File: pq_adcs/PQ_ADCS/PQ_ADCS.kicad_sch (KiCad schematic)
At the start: 55 parts, among them J1 CES-110-02-L-S, J10 Pico-Clasp_01x09, J11 Pico-Clasp_01x15, J12 CES-102-02-L-S, J2 CES-110-02-L-S, J3 CES-110-02-L-S, J4 CES-110-02-L-S, J5 Pico-Clasp_01x03, J6 Pico-Clasp_01x10, J7 Pico-Clasp_01x10, J8 Pico-Clasp_01x10, J9 Pico-Clasp_01x10, U1 LPV542, U2 LPV542, U3 LPV542, U4 IIM-42652, U5 BD2606MVV, U6 TMUX1108RSVR, U7 TCN75AVOA713

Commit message: document formating
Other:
- company: (none) -> NanoSat Lab UPC
- title: (none) -> ADCS subsyetm schematic
- moved on the sheet: C1, C10, C11, C12, C13, C14, C2, C3, C4, C5, C6, C7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

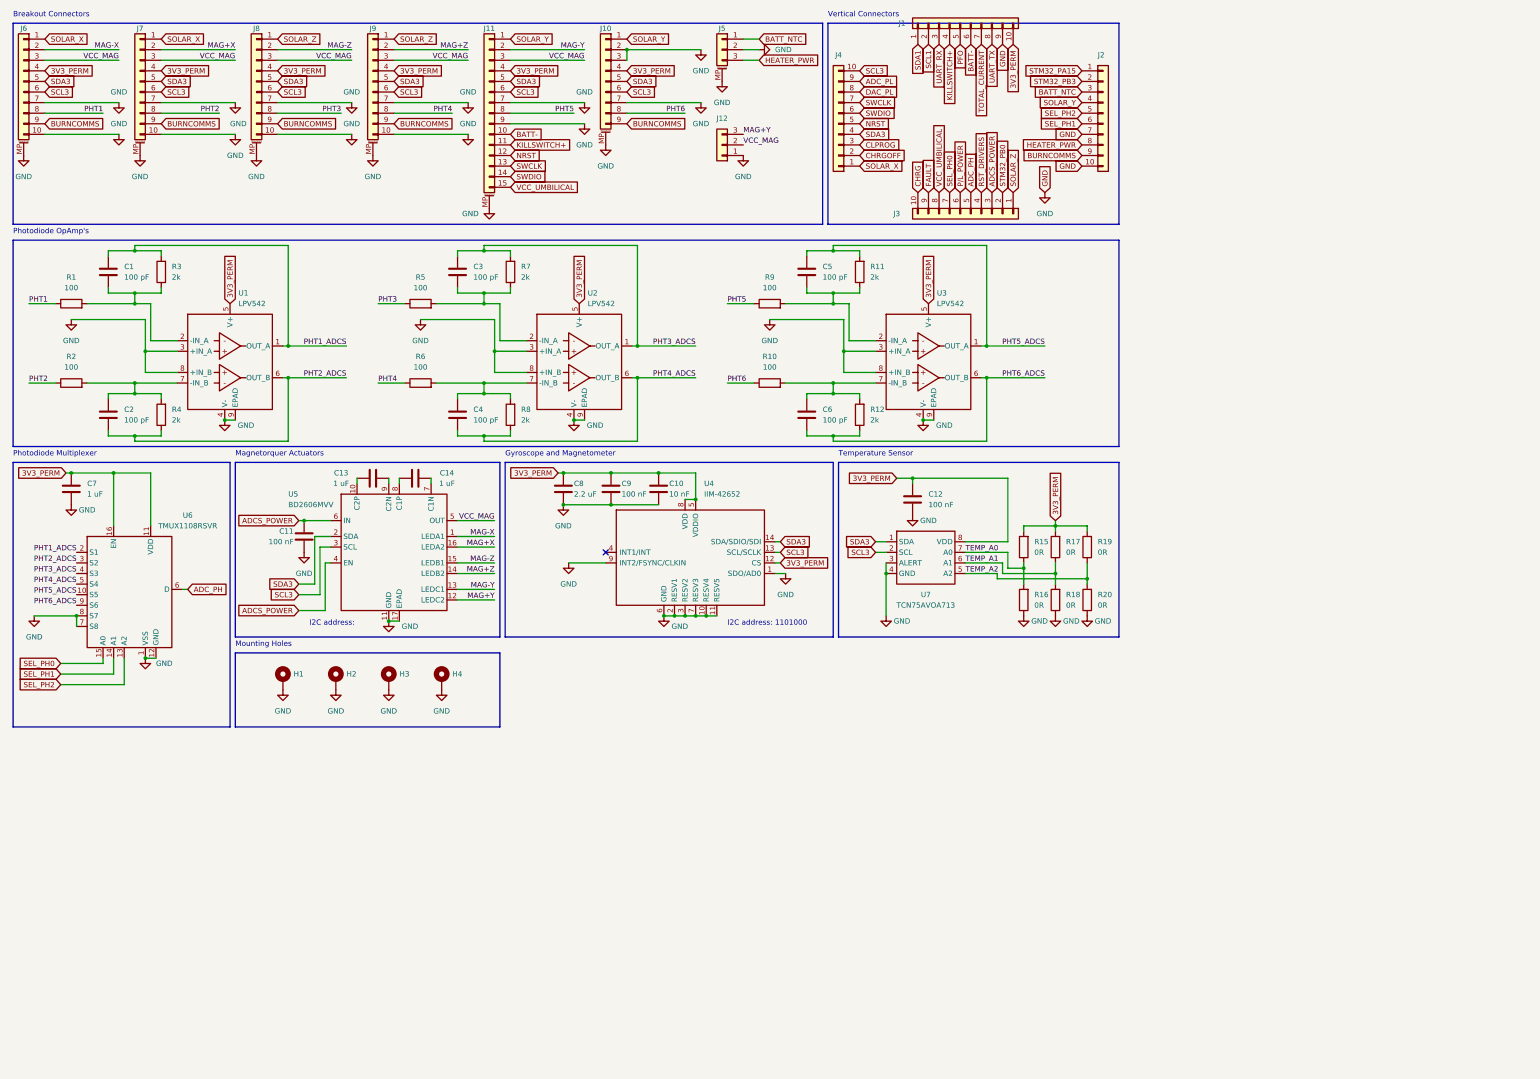
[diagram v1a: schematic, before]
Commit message: ADCS: added magnetometer, removed Tsens. OBC: Total_Current net removed, Bat_NTC routed to PA0 OBC ADC input. Ymag: centering of the vertical pin
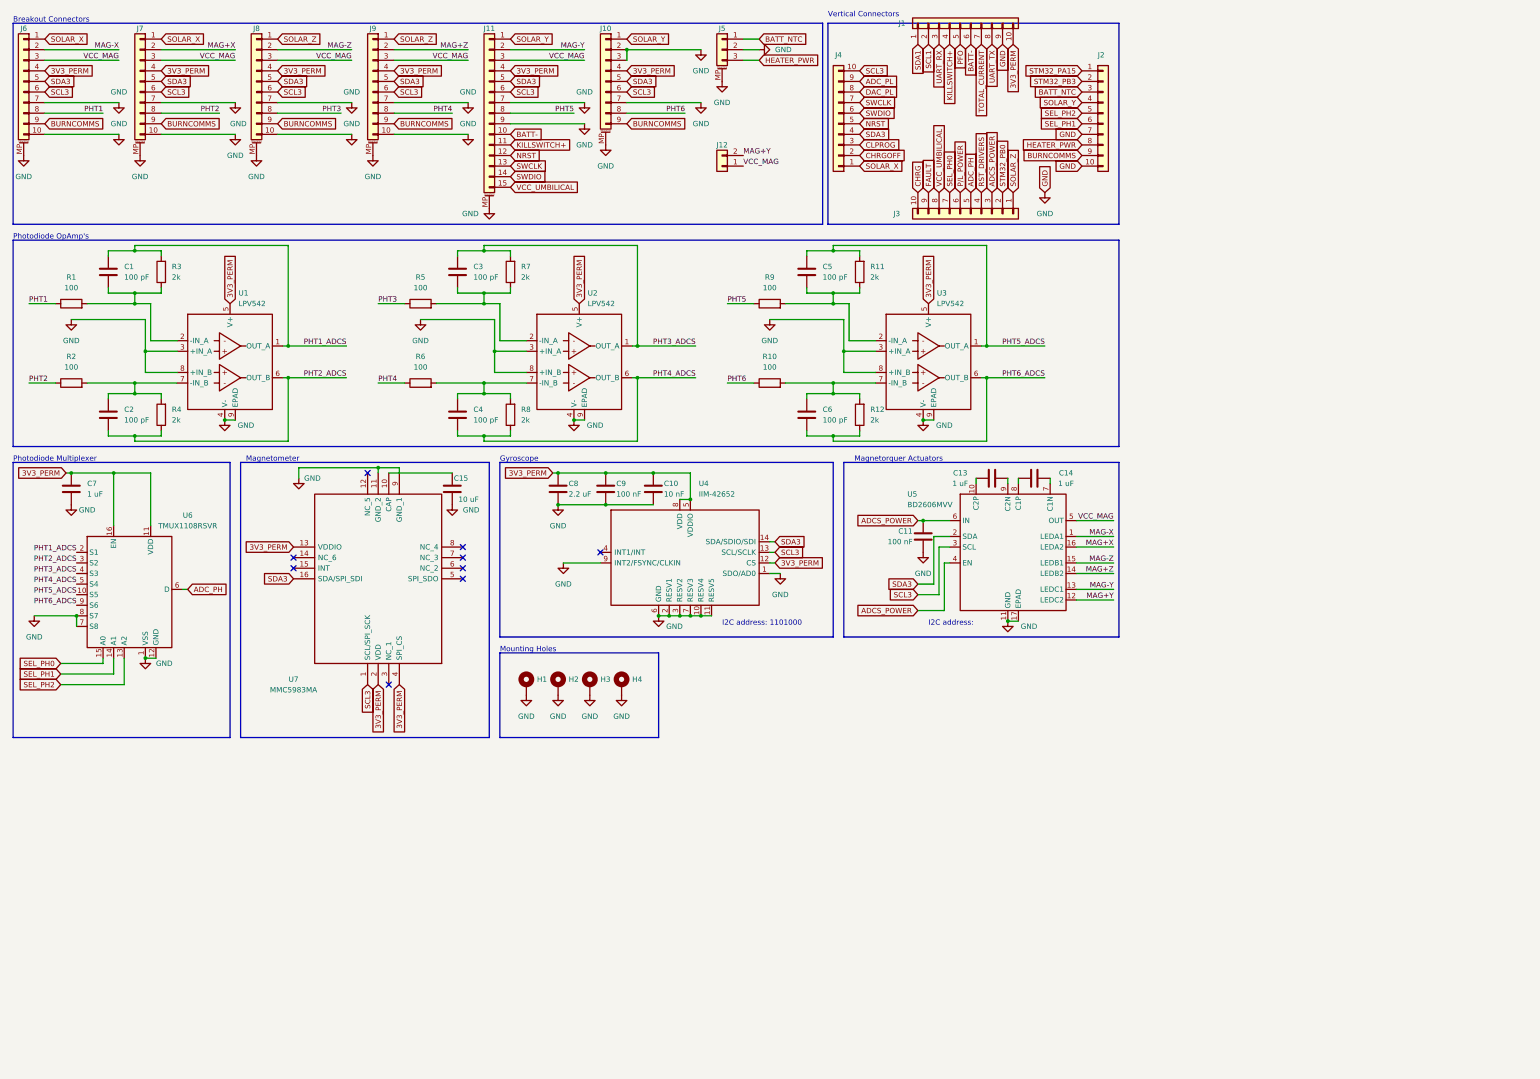
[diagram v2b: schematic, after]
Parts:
- removed C12: 100 nF, Capacitor_SMD:C_0603_1608Metric, symbol Device:C
- removed R15, R16, R17, R18, R19, R20: 0R, Resistor_SMD:R_0402_1005Metric, symbol Device:R
- removed U7: TCN75AVOA713, Package_SO:SOIC-8-1EP_3.9x4.9mm_P1.27mm_EP2.29x3mm, symbol SP_ICs:TCN75AVUA713
- added C15: 10 uF, Capacitor_SMD:C_0603_1608Metric, symbol Device:C
- added U7: MMC5983MA, Package_LGA:LGA-16_3x3mm_P0.5mm, symbol SamacSys_Parts:MMC5983MA
- J12: symbol Connector_Generic:Conn_01x03 -> Connector_Generic:Conn_01x02
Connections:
- net 3V3_PERM: now also U7.13 (VDDIO), U7.2 (VDD), U7.4 (SPI_CS)
- net GND: now also C15.2, U7.11 (GND_2), U7.9 (GND_1); no longer J12.1 (Pin_1)
- net MAG+Y: now also J12.2 (Pin_2); no longer J12.3 (Pin_3)
- net SCL3: now also U7.1 (SCL/SPI_SCK)
- net SDA3: now also U7.16 (SDA/SPI_SDI)
- net VCC_MAG: now also J12.1 (Pin_1); no longer J12.2 (Pin_2)
- new net: C15.1, U7.10 (CAP)
- no-connect marks 1 -> 9
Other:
- note added: "Gyroscope"
- note added: "Magnetometer"
- note removed: "Gyroscope and Magnetometer"
- note removed: "Temperature Sensor"
- moved on the sheet: C10, C11, C13, C14, C8, C9, H1, H2, H3, H4, U4, U5

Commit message: Functional revision and finishing touches part I
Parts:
- added Annotation1: Silkscreen_Annotation, symbols-nsl:Bike, symbol symbols-nsl:Silkscreen_Annotation
- added Annotation2: Silkscreen_Annotation, symbols-nsl:Bridgemaker, symbol symbols-nsl:Silkscreen_Annotation
- U2, U3: footprint GGS_Miscellaneous:TI_X1SON-8_3x3mm -> miscelaneous-nsl:TI_X1SON-8_3x3mm
- U6: footprint GGS_Miscellaneous:UQFN-16_1.8x2.6_Pitch0.4mm -> miscelaneous-nsl:UQFN-16_1.8x2.6_Pitch0.4mm
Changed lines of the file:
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@@
     (pin "2")
+  )
+  (symbol (lib_id "symbols-nsl:Silkscreen_Annotation") (at 252.73 83.82 0) (unit 1)
+    (in_bom yes) (on_board yes) (fields_autoplaced)
+    (property "Reference" "Annotation1" (id 0) (at 259.08 76.8349 0)
+      (effects (font (size 1.27 1.27)) (justify left))
+    )
+    (property "Value" "Silkscreen_Annotation" (id 1) (at 259.08 79.3749 0)
+      (effects (font (size 1.27 1.27)) (justify left))
+    )
+    (property "Footprint" "symbols-nsl:Bike" (id 2) (at 252.73 83.82 0)
+      (effects (font (size 1.27 1.27)) hide)
+    )
+    (property "Datasheet" "" (id 3) (at 252.73 83.82 0)
+      (effects (font (size 1.27 1.27)) hide)
+    )
   )
   (symbol (lib_id "power:GND") (at 233.68 143.51 0) (unit 1)
@@
       (effects (font (size 1.27 1.27)) (justify left))
     )
-    (property "Footprint" "GGS_Miscellaneous:TI_X1SON-8_3x3mm" (id 2) (at 67.31 78.74 0)
+    (property "Footprint" "miscelaneous-nsl:TI_X1SON-8_3x3mm" (id 2) (at 67.31 78.74 0)
       (effects (font (size 1.27 1.27)) hide)
     )
@@
       (effects (font (size 1.27 1.27)) (justify left))
     )
-    (property "Footprint" "GGS_Miscellaneous:TI_X1SON-8_3x3mm" (id 2) (at 234.95 78.74 0)
+    (property "Footprint" "miscelaneous-nsl:TI_X1SON-8_3x3mm" (id 2) (at 234.95 78.74 0)
       (effects (font (size 1.27 1.27)) hide)
     )
@@
       (effects (font (size 1.27 1.27)) (justify left))
     )
-    (property "Footprint" "GGS_Miscellaneous:TI_X1SON-8_3x3mm" (id 2) (at 151.13 78.74 0)
+    (property "Footprint" "miscelaneous-nsl:TI_X1SON-8_3x3mm" (id 2) (at 151.13 78.74 0)
       (effects (font (size 1.27 1.27)) hide)
     )
@@
     )
     (pin "1")
+  )
+  (symbol (lib_id "symbols-nsl:Silkscreen_Annotation") (at 252.73 115.57 0) (unit 1)
+    (in_bom yes) (on_board yes) (fields_autoplaced)
+    (property "Reference" "Annotation2" (id 0) (at 259.08 108.5849 0)
+      (effects (font (size 1.27 1.27)) (justify left))
+    )
+    (property "Value" "Silkscreen_Annotation" (id 1) (at 259.08 111.1249 0)
+      (effects (font (size 1.27 1.27)) (justify left))
+    )
+    (property "Footprint" "symbols-nsl:Bridgemaker" (id 2) (at 252.73 115.57 0)
+      (effects (font (size 1.27 1.27)) hide)
+    )
+    (property "Datasheet" "" (id 3) (at 252.73 115.57 0)
+      (effects (font (size 1.27 1.27)) hide)
+    )
   )
   (symbol (lib_id "Connector_Generic_MountingPin:Conn_01x03_MountingPin") (at 185.42 22.86 0) (mirror y) (unit 1)
@@
     (property "Reference" "U6" (id 0) (at 57.15 134.62 0))
     (property "Value" "TMUX1108RSVR" (id 1) (at 57.15 137.16 0))
-    (property "Footprint" "GGS_Miscellaneous:UQFN-16_1.8x2.6_Pitch0.4mm" (id 2) (at 43.18 181.61 0)
+    (property "Footprint" "miscelaneous-nsl:UQFN-16_1.8x2.6_Pitch0.4mm" (id 2) (at 43.18 181.61 0)
       (effects (font (size 1.27 1.27)) hide)
     )
@@
       (reference "#PWR0128") (unit 1) (value "GND") (footprint "")
     )
+    (path "/39186aee-d768-455f-9f67-07316bbf2442"
+      (reference "Annotation1") (unit 1) (value "Silkscreen_Annotation") (footprint "symbols-nsl:Bike")
+    )
+    (path "/ed472323-2754-430d-9335-9d1815747d4a"
+      (reference "Annotation2") (unit 1) (value "Silkscreen_Annotation") (footprint "symbols-nsl:Bridgemaker")
+    )
     (path "/a9b9c908-a108-4897-b98e-ca718fd00ba8"
       (reference "C1") (unit 1) (value "100 pF") (footprint "Capacitor_SMD:C_0603_1608Metric")
@@
     )
     (path "/5059d6d0-fec7-4fbc-a885-7048f55ac86d"
-      (reference "U1") (unit 1) (value "LPV542") (footprint "GGS_Miscellaneous:TI_X1SON-8_3x3mm")
+      (reference "U1") (unit 1) (value "LPV542") (footprint "miscelaneous-nsl:TI_X1SON-8_3x3mm")
     )
     (path "/c1961d14-6846-4664-b198-f62a3f86b867"
-      (reference "U2") (unit 1) (value "LPV542") (footprint "GGS_Miscellaneous:TI_X1SON-8_3x3mm")
+      (reference "U2") (unit 1) (value "LPV542") (footprint "miscelaneous-nsl:TI_X1SON-8_3x3mm")
     )
     (path "/572489ac-244b-420f-9cd6-18ab497f61b9"
-      (reference "U3") (unit 1) (value "LPV542") (footprint "GGS_Miscellaneous:TI_X1SON-8_3x3mm")
+      (reference "U3") (unit 1) (value "LPV542") (footprint "miscelaneous-nsl:TI_X1SON-8_3x3mm")
     )
     (path "/10f02a1c-802b-491a-b0a5-6ceb0f16f545"
@@
     )
     (path "/f6323bc2-5c02-4cce-8ed7-f8d4b30b275b"
-      (reference "U6") (unit 1) (value "TMUX1108RSVR") (footprint "GGS_Miscellaneous:UQFN-16_1.8x2.6_Pitch0.4mm")
+      (reference "U6") (unit 1) (value "TMUX1108RSVR") (footprint "miscelaneous-nsl:UQFN-16_1.8x2.6_Pitch0.4mm")
     )
     (path "/2e84e1cc-1a7b-4bb7-82f4-997821b68f05"

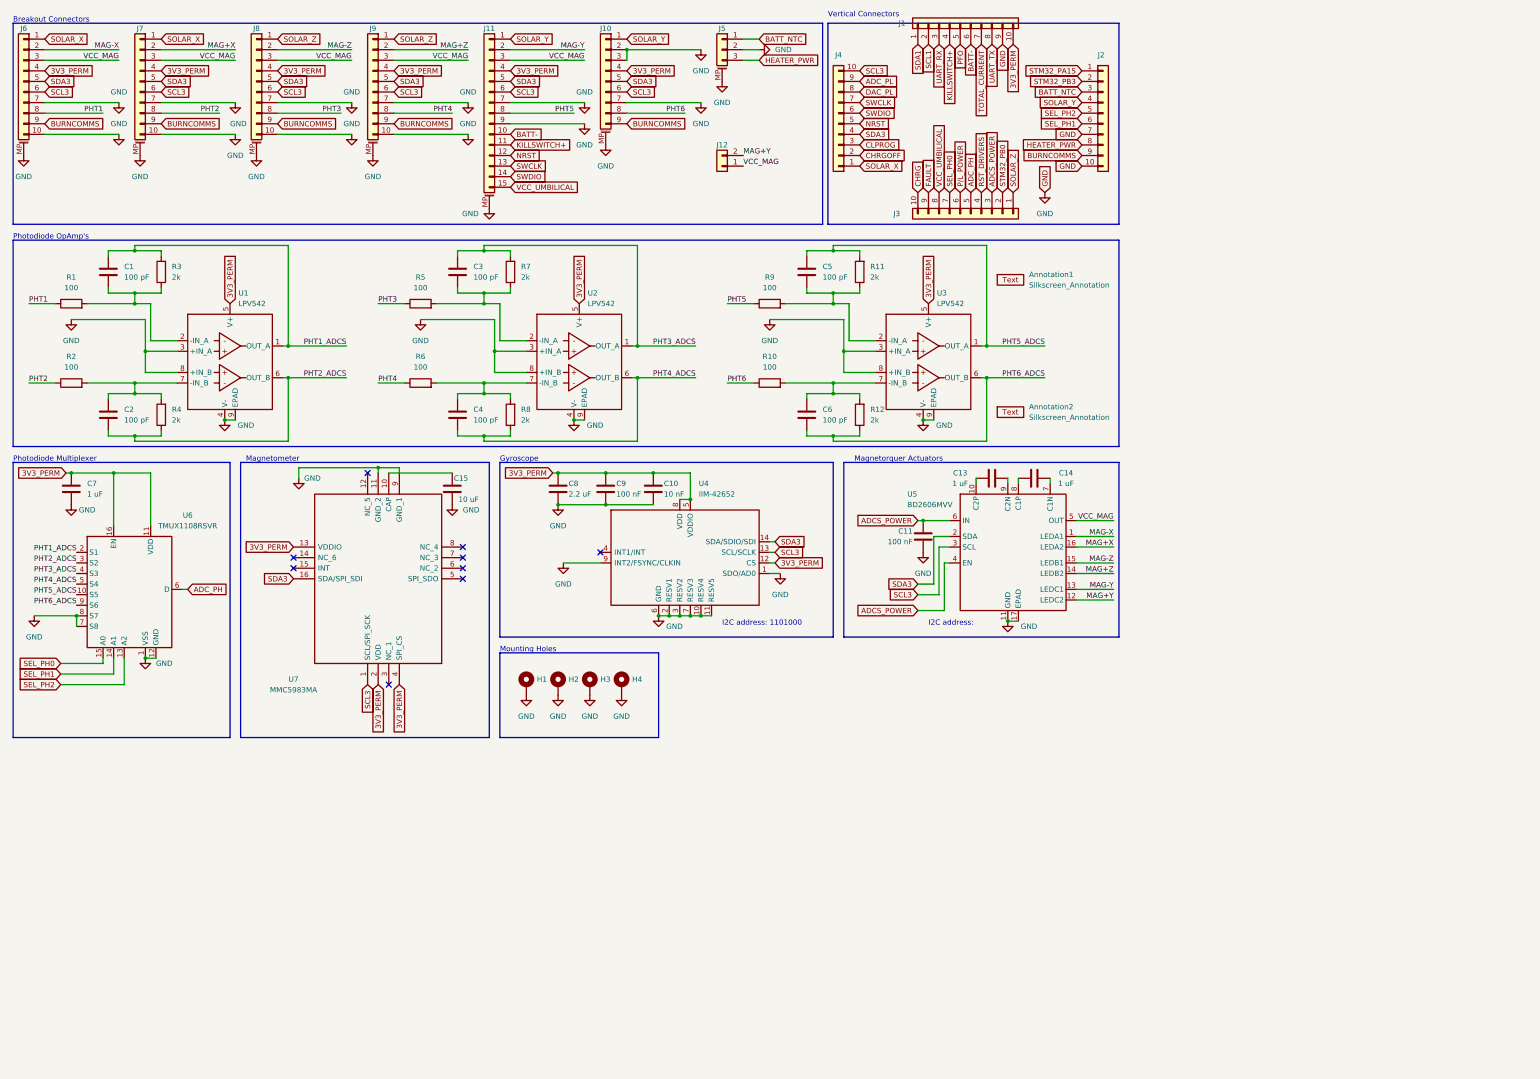
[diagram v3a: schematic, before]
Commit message: Full Kicad7 transition, library improvement and adaptation, correct footprints and 3D models added
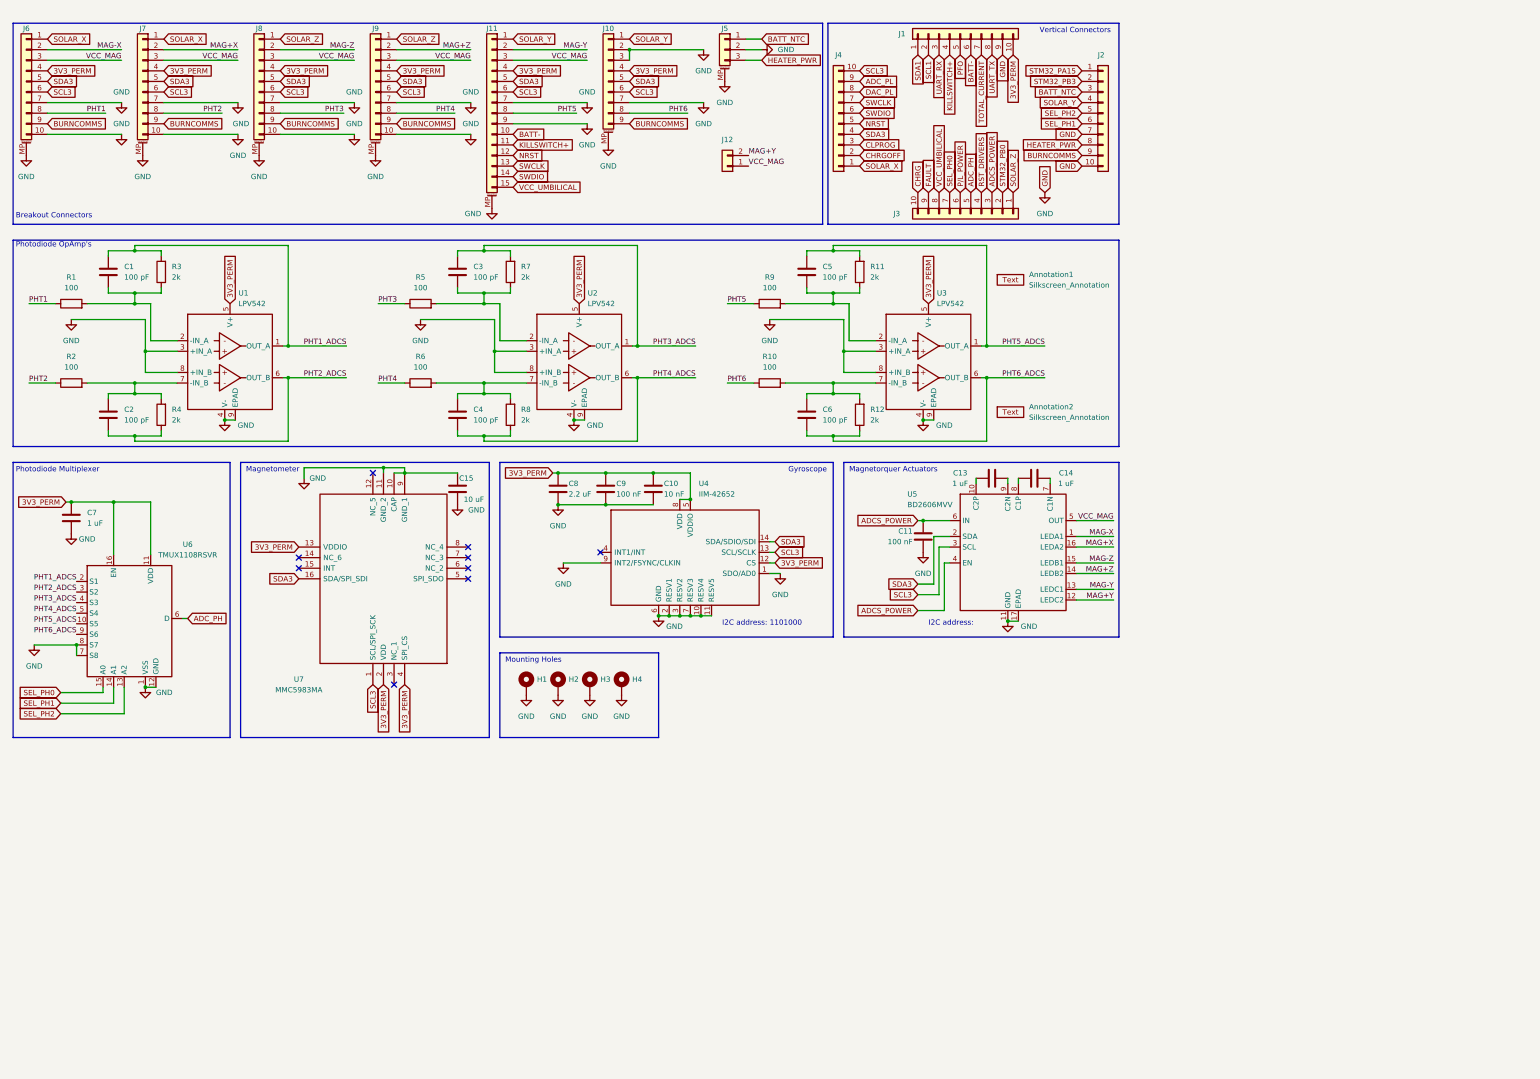
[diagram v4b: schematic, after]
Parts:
- Annotation1: footprint symbols-nsl:Bike -> -nsl_symbols:Bike
- Annotation2: footprint symbols-nsl:Bridgemaker -> -nsl_symbols:Bridgemaker
- J1, J2, J3, J4: footprint Connector_PinSocket_2.54mm:PinSocket_1x10_P2.54mm_Vertical -> -nsl_connector:SLW-110-01
- J10: footprint Connector_Molex:Molex_Pico-Clasp_202396-0907_1x09-1MP_P1.00mm_Horizontal -> -nsl_connector:Picoclasp09; symbol Connector_Generic_MountingPin:Conn_01x09_MountingPin -> -nsl_connector:Picoclasp09
- J11: footprint Connector_Molex:Molex_Pico-Clasp_202396-1507_1x15-1MP_P1.00mm_Horizontal -> -nsl_connector:Picoclasp15; symbol Connector_Generic_MountingPin:Conn_01x15_MountingPin -> -nsl_connector:Picoclasp15
- J12: footprint Connector_PinHeader_2.54mm:PinHeader_1x02_P2.54mm_Vertical -> -nsl_connector:CES-102-02; symbol Connector_Generic:Conn_01x02 -> -nsl_connector:CES-102-02
- J5: footprint Connector_Molex:Molex_Pico-Clasp_202396-0307_1x03-1MP_P1.00mm_Horizontal -> -nsl_connector:Picoclasp03; symbol Connector_Generic_MountingPin:Conn_01x03_MountingPin -> -nsl_connector:Picoclasp03
- J6, J7, J8, J9: footprint Connector_Molex:Molex_Pico-Clasp_202396-1007_1x10-1MP_P1.00mm_Horizontal -> -nsl_connector:Picoclasp10; symbol Connector_Generic_MountingPin:Conn_01x10_MountingPin -> -nsl_connector:Picoclasp10
- U2, U3: footprint miscelaneous-nsl:TI_X1SON-8_3x3mm -> -nsl_miscellaneous:TI_X1SON-8_3x3mm
- U6: footprint miscelaneous-nsl:UQFN-16_1.8x2.6_Pitch0.4mm -> -nsl_miscellaneous:UQFN-16_1.8x2.6_Pitch0.4mm
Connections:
- net GND: now also C15.1, U7.10 (CAP)
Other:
- moved on the sheet: C15, C7, J1, J10, J11, J12, J5, J6, J7, J8, J9, U6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
